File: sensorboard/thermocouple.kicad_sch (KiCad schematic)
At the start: 8 parts, among them U16 MAX31856

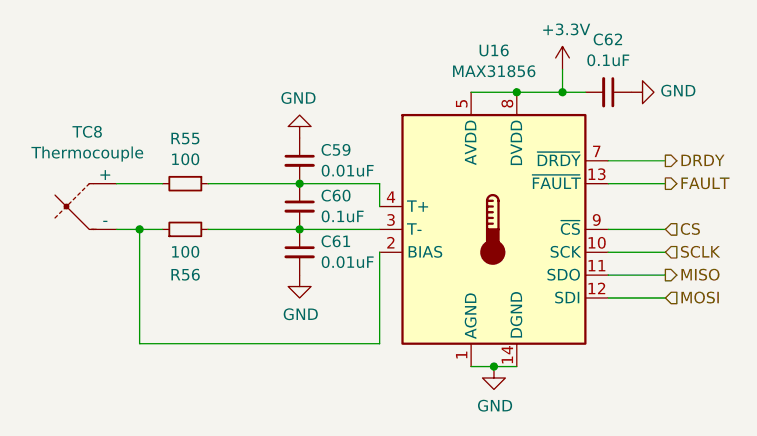
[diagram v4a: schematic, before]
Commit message: rearranged CAN and boost converter
LEDs moved
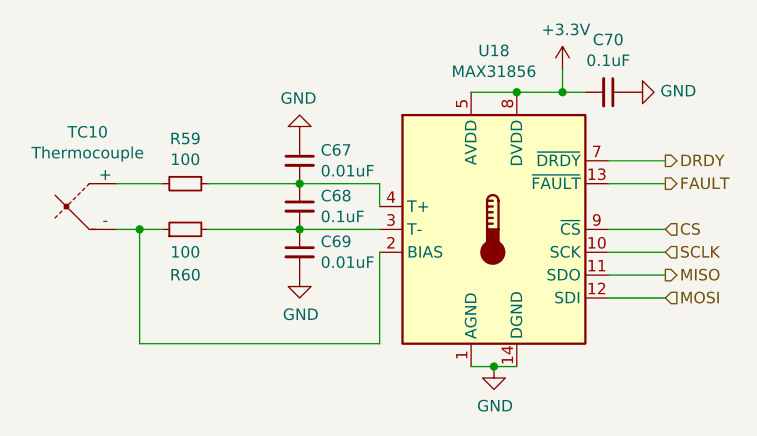
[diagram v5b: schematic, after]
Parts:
- renumbered C59 to C67, C60 to C68, C61 to C69, C62 to C70, R55 to R59, R56 to R60, TC8 to TC10, U16 to U18
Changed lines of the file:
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@@
   (symbol (lib_id "Sensor_Temperature:MAX31856") (at 95.25 73.66 0)
     (in_bom yes) (on_board yes)
-    (property "Reference" "U16" (id 0) (at 95.25 53.8226 0))
+    (property "Reference" "U18" (id 0) (at 95.25 53.8226 0))
     (property "Value" "MAX31856" (id 1) (at 95.25 56.134 0))
     (property "Footprint" "Package_SO:TSSOP-14_4.4x5mm_P0.65mm" (id 2) (at 99.06 87.63 0)
@@
   (symbol (lib_id "power:GND") (at 95.25 88.9 0)
     (in_bom yes) (on_board yes)
-    (property "Reference" "#PWR0120" (id 0) (at 95.25 95.25 0)
+    (property "Reference" "#PWR0130" (id 0) (at 95.25 95.25 0)
       (effects (font (size 1.27 1.27)) hide)
     )
@@
   (symbol (lib_id "analogue-cache:+3.3V") (at 102.87 55.88 0)
     (in_bom yes) (on_board yes)
-    (property "Reference" "#PWR0121" (id 0) (at 102.87 59.69 0)
+    (property "Reference" "#PWR0131" (id 0) (at 102.87 59.69 0)
       (effects (font (size 1.27 1.27)) hide)
     )
@@
   (symbol (lib_id "Device:C_Small") (at 107.95 58.42 270)
     (in_bom yes) (on_board yes)
-    (property "Reference" "C62" (id 0) (at 107.95 52.6034 90))
+    (property "Reference" "C70" (id 0) (at 107.95 52.6034 90))
     (property "Value" "0.1uF" (id 1) (at 107.95 54.9148 90))
     (property "Footprint" "Capacitor_SMD:C_0603_1608Metric" (id 2) (at 107.95 58.42 0)
@@
   (symbol (lib_id "power:GND") (at 110.49 58.42 90)
     (in_bom yes) (on_board yes)
-    (property "Reference" "#PWR0122" (id 0) (at 116.84 58.42 0)
+    (property "Reference" "#PWR0132" (id 0) (at 116.84 58.42 0)
       (effects (font (size 1.27 1.27)) hide)
     )
@@
   (symbol (lib_id "Device:Thermocouple") (at 50.8 71.12 0)
     (in_bom yes) (on_board yes)
-    (property "Reference" "TC8" (id 0) (at 50.1142 62.865 0))
+    (property "Reference" "TC10" (id 0) (at 50.1142 62.865 0))
     (property "Value" "Thermocouple" (id 1) (at 50.1142 65.1764 0))
     (property "Footprint" "TerminalBlock_TE-Connectivity:TerminalBlock_TE_282834-2_1x02_P2.54mm_Horizontal" (id 2) (at 36.195 69.85 0)
@@
   (symbol (lib_id "Device:R_Small") (at 60.96 68.58 270)
     (in_bom yes) (on_board yes)
-    (property "Reference" "R55" (id 0) (at 60.96 63.6016 90))
+    (property "Reference" "R59" (id 0) (at 60.96 63.6016 90))
     (property "Value" "100" (id 1) (at 60.96 65.913 90))
     (property "Footprint" "Resistor_SMD:R_0603_1608Metric" (id 2) (at 60.96 68.58 0)
@@
   (symbol (lib_id "Device:R_Small") (at 60.96 73.66 90)
     (in_bom yes) (on_board yes)
-    (property "Reference" "R56" (id 0) (at 60.96 78.74 90))
+    (property "Reference" "R60" (id 0) (at 60.96 78.74 90))
     (property "Value" "100" (id 1) (at 60.96 76.2 90))
     (property "Footprint" "Resistor_SMD:R_0603_1608Metric" (id 2) (at 60.96 73.66 0)
@@
   (symbol (lib_id "Device:C_Small") (at 73.66 71.12 0)
     (in_bom yes) (on_board yes)
-    (property "Reference" "C60" (id 0) (at 75.9968 69.9516 0)
+    (property "Reference" "C68" (id 0) (at 75.9968 69.9516 0)
       (effects (font (size 1.27 1.27)) (justify left))
     )
@@
   (symbol (lib_id "Device:C_Small") (at 73.66 66.04 0)
     (in_bom yes) (on_board yes)
-    (property "Reference" "C59" (id 0) (at 75.9968 64.8716 0)
+    (property "Reference" "C67" (id 0) (at 75.9968 64.8716 0)
       (effects (font (size 1.27 1.27)) (justify left))
     )
@@
   (symbol (lib_id "Device:C_Small") (at 73.66 76.2 0)
     (in_bom yes) (on_board yes)
-    (property "Reference" "C61" (id 0) (at 75.9968 75.0316 0)
+    (property "Reference" "C69" (id 0) (at 75.9968 75.0316 0)
       (effects (font (size 1.27 1.27)) (justify left))
     )
@@
   (symbol (lib_id "power:GND") (at 73.66 78.74 0)
     (in_bom yes) (on_board yes)
-    (property "Reference" "#PWR0119" (id 0) (at 73.66 85.09 0)
+    (property "Reference" "#PWR0129" (id 0) (at 73.66 85.09 0)
       (effects (font (size 1.27 1.27)) hide)
     )
@@
   (symbol (lib_id "power:GND") (at 73.66 63.5 180)
     (in_bom yes) (on_board yes)
-    (property "Reference" "#PWR0118" (id 0) (at 73.66 57.15 0)
+    (property "Reference" "#PWR0128" (id 0) (at 73.66 57.15 0)
       (effects (font (size 1.27 1.27)) hide)
     )

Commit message: Update thermocouple connection
changed schematic (c55 --> cs5) and positions. Copies made
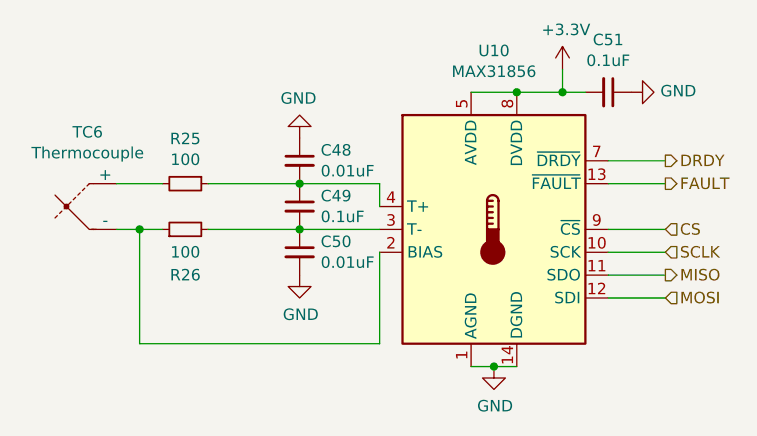
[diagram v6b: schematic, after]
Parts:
- renumbered C67 to C48, C68 to C49, C69 to C50, C70 to C51, R59 to R25, R60 to R26, TC10 to TC6, U18 to U10
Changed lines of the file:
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@@
   (symbol (lib_id "Sensor_Temperature:MAX31856") (at 95.25 73.66 0)
     (in_bom yes) (on_board yes)
-    (property "Reference" "U18" (id 0) (at 95.25 53.8226 0))
+    (property "Reference" "U10" (id 0) (at 95.25 53.8226 0))
     (property "Value" "MAX31856" (id 1) (at 95.25 56.134 0))
     (property "Footprint" "Package_SO:TSSOP-14_4.4x5mm_P0.65mm" (id 2) (at 99.06 87.63 0)
@@
   (symbol (lib_id "power:GND") (at 95.25 88.9 0)
     (in_bom yes) (on_board yes)
-    (property "Reference" "#PWR0130" (id 0) (at 95.25 95.25 0)
+    (property "Reference" "#PWR058" (id 0) (at 95.25 95.25 0)
       (effects (font (size 1.27 1.27)) hide)
     )
@@
   (symbol (lib_id "analogue-cache:+3.3V") (at 102.87 55.88 0)
     (in_bom yes) (on_board yes)
-    (property "Reference" "#PWR0131" (id 0) (at 102.87 59.69 0)
+    (property "Reference" "#PWR060" (id 0) (at 102.87 59.69 0)
       (effects (font (size 1.27 1.27)) hide)
     )
@@
   (symbol (lib_id "Device:C_Small") (at 107.95 58.42 270)
     (in_bom yes) (on_board yes)
-    (property "Reference" "C70" (id 0) (at 107.95 52.6034 90))
+    (property "Reference" "C51" (id 0) (at 107.95 52.6034 90))
     (property "Value" "0.1uF" (id 1) (at 107.95 54.9148 90))
     (property "Footprint" "Capacitor_SMD:C_0603_1608Metric" (id 2) (at 107.95 58.42 0)
@@
   (symbol (lib_id "power:GND") (at 110.49 58.42 90)
     (in_bom yes) (on_board yes)
-    (property "Reference" "#PWR0132" (id 0) (at 116.84 58.42 0)
+    (property "Reference" "#PWR061" (id 0) (at 116.84 58.42 0)
       (effects (font (size 1.27 1.27)) hide)
     )
@@
   (symbol (lib_id "Device:Thermocouple") (at 50.8 71.12 0)
     (in_bom yes) (on_board yes)
-    (property "Reference" "TC10" (id 0) (at 50.1142 62.865 0))
+    (property "Reference" "TC6" (id 0) (at 50.1142 62.865 0))
     (property "Value" "Thermocouple" (id 1) (at 50.1142 65.1764 0))
     (property "Footprint" "TerminalBlock_TE-Connectivity:TerminalBlock_TE_282834-2_1x02_P2.54mm_Horizontal" (id 2) (at 36.195 69.85 0)
@@
   (symbol (lib_id "Device:R_Small") (at 60.96 68.58 270)
     (in_bom yes) (on_board yes)
-    (property "Reference" "R59" (id 0) (at 60.96 63.6016 90))
+    (property "Reference" "R25" (id 0) (at 60.96 63.6016 90))
     (property "Value" "100" (id 1) (at 60.96 65.913 90))
     (property "Footprint" "Resistor_SMD:R_0603_1608Metric" (id 2) (at 60.96 68.58 0)
@@
   (symbol (lib_id "Device:R_Small") (at 60.96 73.66 90)
     (in_bom yes) (on_board yes)
-    (property "Reference" "R60" (id 0) (at 60.96 78.74 90))
+    (property "Reference" "R26" (id 0) (at 60.96 78.74 90))
     (property "Value" "100" (id 1) (at 60.96 76.2 90))
     (property "Footprint" "Resistor_SMD:R_0603_1608Metric" (id 2) (at 60.96 73.66 0)
@@
   (symbol (lib_id "Device:C_Small") (at 73.66 71.12 0)
     (in_bom yes) (on_board yes)
-    (property "Reference" "C68" (id 0) (at 75.9968 69.9516 0)
+    (property "Reference" "C49" (id 0) (at 75.9968 69.9516 0)
       (effects (font (size 1.27 1.27)) (justify left))
     )
@@
   (symbol (lib_id "Device:C_Small") (at 73.66 66.04 0)
     (in_bom yes) (on_board yes)
-    (property "Reference" "C67" (id 0) (at 75.9968 64.8716 0)
+    (property "Reference" "C48" (id 0) (at 75.9968 64.8716 0)
       (effects (font (size 1.27 1.27)) (justify left))
     )
@@
   (symbol (lib_id "Device:C_Small") (at 73.66 76.2 0)
     (in_bom yes) (on_board yes)
-    (property "Reference" "C69" (id 0) (at 75.9968 75.0316 0)
+    (property "Reference" "C50" (id 0) (at 75.9968 75.0316 0)
       (effects (font (size 1.27 1.27)) (justify left))
     )
@@
   (symbol (lib_id "power:GND") (at 73.66 78.74 0)
     (in_bom yes) (on_board yes)
-    (property "Reference" "#PWR0129" (id 0) (at 73.66 85.09 0)
+    (property "Reference" "#PWR057" (id 0) (at 73.66 85.09 0)
       (effects (font (size 1.27 1.27)) hide)
     )
@@
   (symbol (lib_id "power:GND") (at 73.66 63.5 180)
     (in_bom yes) (on_board yes)
-    (property "Reference" "#PWR0128" (id 0) (at 73.66 57.15 0)
+    (property "Reference" "#PWR056" (id 0) (at 73.66 57.15 0)
       (effects (font (size 1.27 1.27)) hide)
     )

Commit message: Integrated in USB and CAN
CAN_TX and CAN_RX are moved
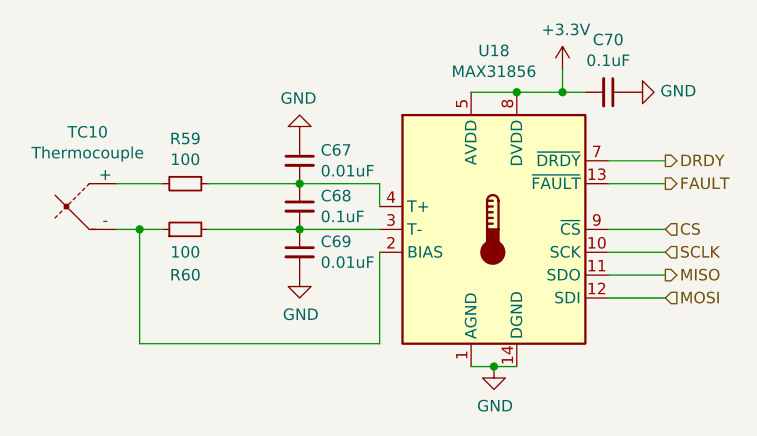
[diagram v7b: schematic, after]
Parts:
- renumbered C48 to C67, C49 to C68, C50 to C69, C51 to C70, R25 to R59, R26 to R60, TC6 to TC10, U10 to U18
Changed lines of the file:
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@@
   (symbol (lib_id "Sensor_Temperature:MAX31856") (at 95.25 73.66 0)
     (in_bom yes) (on_board yes)
-    (property "Reference" "U10" (id 0) (at 95.25 53.8226 0))
+    (property "Reference" "U18" (id 0) (at 95.25 53.8226 0))
     (property "Value" "MAX31856" (id 1) (at 95.25 56.134 0))
     (property "Footprint" "Package_SO:TSSOP-14_4.4x5mm_P0.65mm" (id 2) (at 99.06 87.63 0)
@@
   (symbol (lib_id "power:GND") (at 95.25 88.9 0)
     (in_bom yes) (on_board yes)
-    (property "Reference" "#PWR058" (id 0) (at 95.25 95.25 0)
+    (property "Reference" "#PWR0130" (id 0) (at 95.25 95.25 0)
       (effects (font (size 1.27 1.27)) hide)
     )
@@
   (symbol (lib_id "analogue-cache:+3.3V") (at 102.87 55.88 0)
     (in_bom yes) (on_board yes)
-    (property "Reference" "#PWR060" (id 0) (at 102.87 59.69 0)
+    (property "Reference" "#PWR0131" (id 0) (at 102.87 59.69 0)
       (effects (font (size 1.27 1.27)) hide)
     )
@@
   (symbol (lib_id "Device:C_Small") (at 107.95 58.42 270)
     (in_bom yes) (on_board yes)
-    (property "Reference" "C51" (id 0) (at 107.95 52.6034 90))
+    (property "Reference" "C70" (id 0) (at 107.95 52.6034 90))
     (property "Value" "0.1uF" (id 1) (at 107.95 54.9148 90))
     (property "Footprint" "Capacitor_SMD:C_0603_1608Metric" (id 2) (at 107.95 58.42 0)
@@
   (symbol (lib_id "power:GND") (at 110.49 58.42 90)
     (in_bom yes) (on_board yes)
-    (property "Reference" "#PWR061" (id 0) (at 116.84 58.42 0)
+    (property "Reference" "#PWR0132" (id 0) (at 116.84 58.42 0)
       (effects (font (size 1.27 1.27)) hide)
     )
@@
   (symbol (lib_id "Device:Thermocouple") (at 50.8 71.12 0)
     (in_bom yes) (on_board yes)
-    (property "Reference" "TC6" (id 0) (at 50.1142 62.865 0))
+    (property "Reference" "TC10" (id 0) (at 50.1142 62.865 0))
     (property "Value" "Thermocouple" (id 1) (at 50.1142 65.1764 0))
     (property "Footprint" "TerminalBlock_TE-Connectivity:TerminalBlock_TE_282834-2_1x02_P2.54mm_Horizontal" (id 2) (at 36.195 69.85 0)
@@
   (symbol (lib_id "Device:R_Small") (at 60.96 68.58 270)
     (in_bom yes) (on_board yes)
-    (property "Reference" "R25" (id 0) (at 60.96 63.6016 90))
+    (property "Reference" "R59" (id 0) (at 60.96 63.6016 90))
     (property "Value" "100" (id 1) (at 60.96 65.913 90))
     (property "Footprint" "Resistor_SMD:R_0603_1608Metric" (id 2) (at 60.96 68.58 0)
@@
   (symbol (lib_id "Device:R_Small") (at 60.96 73.66 90)
     (in_bom yes) (on_board yes)
-    (property "Reference" "R26" (id 0) (at 60.96 78.74 90))
+    (property "Reference" "R60" (id 0) (at 60.96 78.74 90))
     (property "Value" "100" (id 1) (at 60.96 76.2 90))
     (property "Footprint" "Resistor_SMD:R_0603_1608Metric" (id 2) (at 60.96 73.66 0)
@@
   (symbol (lib_id "Device:C_Small") (at 73.66 71.12 0)
     (in_bom yes) (on_board yes)
-    (property "Reference" "C49" (id 0) (at 75.9968 69.9516 0)
+    (property "Reference" "C68" (id 0) (at 75.9968 69.9516 0)
       (effects (font (size 1.27 1.27)) (justify left))
     )
@@
   (symbol (lib_id "Device:C_Small") (at 73.66 66.04 0)
     (in_bom yes) (on_board yes)
-    (property "Reference" "C48" (id 0) (at 75.9968 64.8716 0)
+    (property "Reference" "C67" (id 0) (at 75.9968 64.8716 0)
       (effects (font (size 1.27 1.27)) (justify left))
     )
@@
   (symbol (lib_id "Device:C_Small") (at 73.66 76.2 0)
     (in_bom yes) (on_board yes)
-    (property "Reference" "C50" (id 0) (at 75.9968 75.0316 0)
+    (property "Reference" "C69" (id 0) (at 75.9968 75.0316 0)
       (effects (font (size 1.27 1.27)) (justify left))
     )
@@
   (symbol (lib_id "power:GND") (at 73.66 78.74 0)
     (in_bom yes) (on_board yes)
-    (property "Reference" "#PWR057" (id 0) (at 73.66 85.09 0)
+    (property "Reference" "#PWR0129" (id 0) (at 73.66 85.09 0)
       (effects (font (size 1.27 1.27)) hide)
     )
@@
   (symbol (lib_id "power:GND") (at 73.66 63.5 180)
     (in_bom yes) (on_board yes)
-    (property "Reference" "#PWR056" (id 0) (at 73.66 57.15 0)
+    (property "Reference" "#PWR0128" (id 0) (at 73.66 57.15 0)
       (effects (font (size 1.27 1.27)) hide)
     )

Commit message: changed BOOT pin, auto reset caps
moved references about
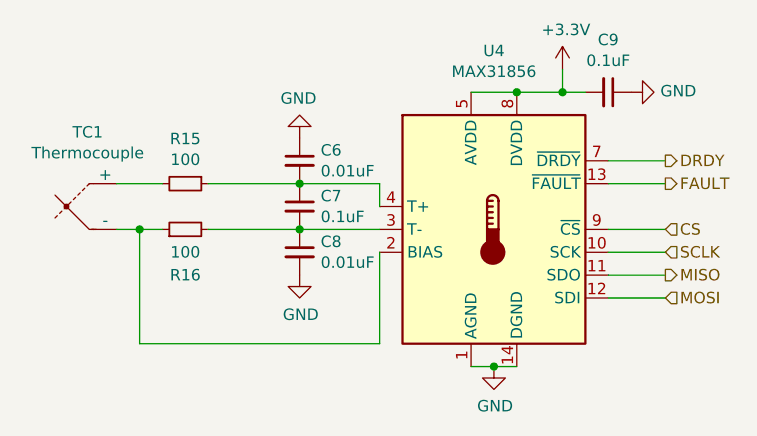
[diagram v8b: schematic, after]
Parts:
- renumbered C67 to C6, C68 to C7, C69 to C8, C70 to C9, R59 to R15, R60 to R16, TC10 to TC1, U18 to U4
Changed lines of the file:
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@@
   (symbol (lib_id "Sensor_Temperature:MAX31856") (at 95.25 73.66 0)
     (in_bom yes) (on_board yes)
-    (property "Reference" "U18" (id 0) (at 95.25 53.8226 0))
+    (property "Reference" "U4" (id 0) (at 95.25 53.8226 0))
     (property "Value" "MAX31856" (id 1) (at 95.25 56.134 0))
     (property "Footprint" "Package_SO:TSSOP-14_4.4x5mm_P0.65mm" (id 2) (at 99.06 87.63 0)
@@
   (symbol (lib_id "Device:C_Small") (at 107.95 58.42 270)
     (in_bom yes) (on_board yes)
-    (property "Reference" "C70" (id 0) (at 107.95 52.6034 90))
+    (property "Reference" "C9" (id 0) (at 107.95 52.6034 90))
     (property "Value" "0.1uF" (id 1) (at 107.95 54.9148 90))
     (property "Footprint" "Capacitor_SMD:C_0603_1608Metric" (id 2) (at 107.95 58.42 0)
@@
   (symbol (lib_id "Device:Thermocouple") (at 50.8 71.12 0)
     (in_bom yes) (on_board yes)
-    (property "Reference" "TC10" (id 0) (at 50.1142 62.865 0))
+    (property "Reference" "TC1" (id 0) (at 50.1142 62.865 0))
     (property "Value" "Thermocouple" (id 1) (at 50.1142 65.1764 0))
     (property "Footprint" "TerminalBlock_TE-Connectivity:TerminalBlock_TE_282834-2_1x02_P2.54mm_Horizontal" (id 2) (at 36.195 69.85 0)
@@
   (symbol (lib_id "Device:R_Small") (at 60.96 68.58 270)
     (in_bom yes) (on_board yes)
-    (property "Reference" "R59" (id 0) (at 60.96 63.6016 90))
+    (property "Reference" "R15" (id 0) (at 60.96 63.6016 90))
     (property "Value" "100" (id 1) (at 60.96 65.913 90))
     (property "Footprint" "Resistor_SMD:R_0603_1608Metric" (id 2) (at 60.96 68.58 0)
@@
   (symbol (lib_id "Device:R_Small") (at 60.96 73.66 90)
     (in_bom yes) (on_board yes)
-    (property "Reference" "R60" (id 0) (at 60.96 78.74 90))
+    (property "Reference" "R16" (id 0) (at 60.96 78.74 90))
     (property "Value" "100" (id 1) (at 60.96 76.2 90))
     (property "Footprint" "Resistor_SMD:R_0603_1608Metric" (id 2) (at 60.96 73.66 0)
@@
   (symbol (lib_id "Device:C_Small") (at 73.66 71.12 0)
     (in_bom yes) (on_board yes)
-    (property "Reference" "C68" (id 0) (at 75.9968 69.9516 0)
+    (property "Reference" "C7" (id 0) (at 75.9968 69.9516 0)
       (effects (font (size 1.27 1.27)) (justify left))
     )
@@
   (symbol (lib_id "Device:C_Small") (at 73.66 66.04 0)
     (in_bom yes) (on_board yes)
-    (property "Reference" "C67" (id 0) (at 75.9968 64.8716 0)
+    (property "Reference" "C6" (id 0) (at 75.9968 64.8716 0)
       (effects (font (size 1.27 1.27)) (justify left))
     )
@@
   (symbol (lib_id "Device:C_Small") (at 73.66 76.2 0)
     (in_bom yes) (on_board yes)
-    (property "Reference" "C69" (id 0) (at 75.9968 75.0316 0)
+    (property "Reference" "C8" (id 0) (at 75.9968 75.0316 0)
       (effects (font (size 1.27 1.27)) (justify left))
     )
